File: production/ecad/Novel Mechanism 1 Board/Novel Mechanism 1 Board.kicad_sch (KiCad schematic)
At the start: 29 parts, among them J3 0532611271, U1 ADC081C021CIMM/NOPB, U2 ADC081C021CIMM/NOPB, U3 ADC081C021CIMM/NOPB

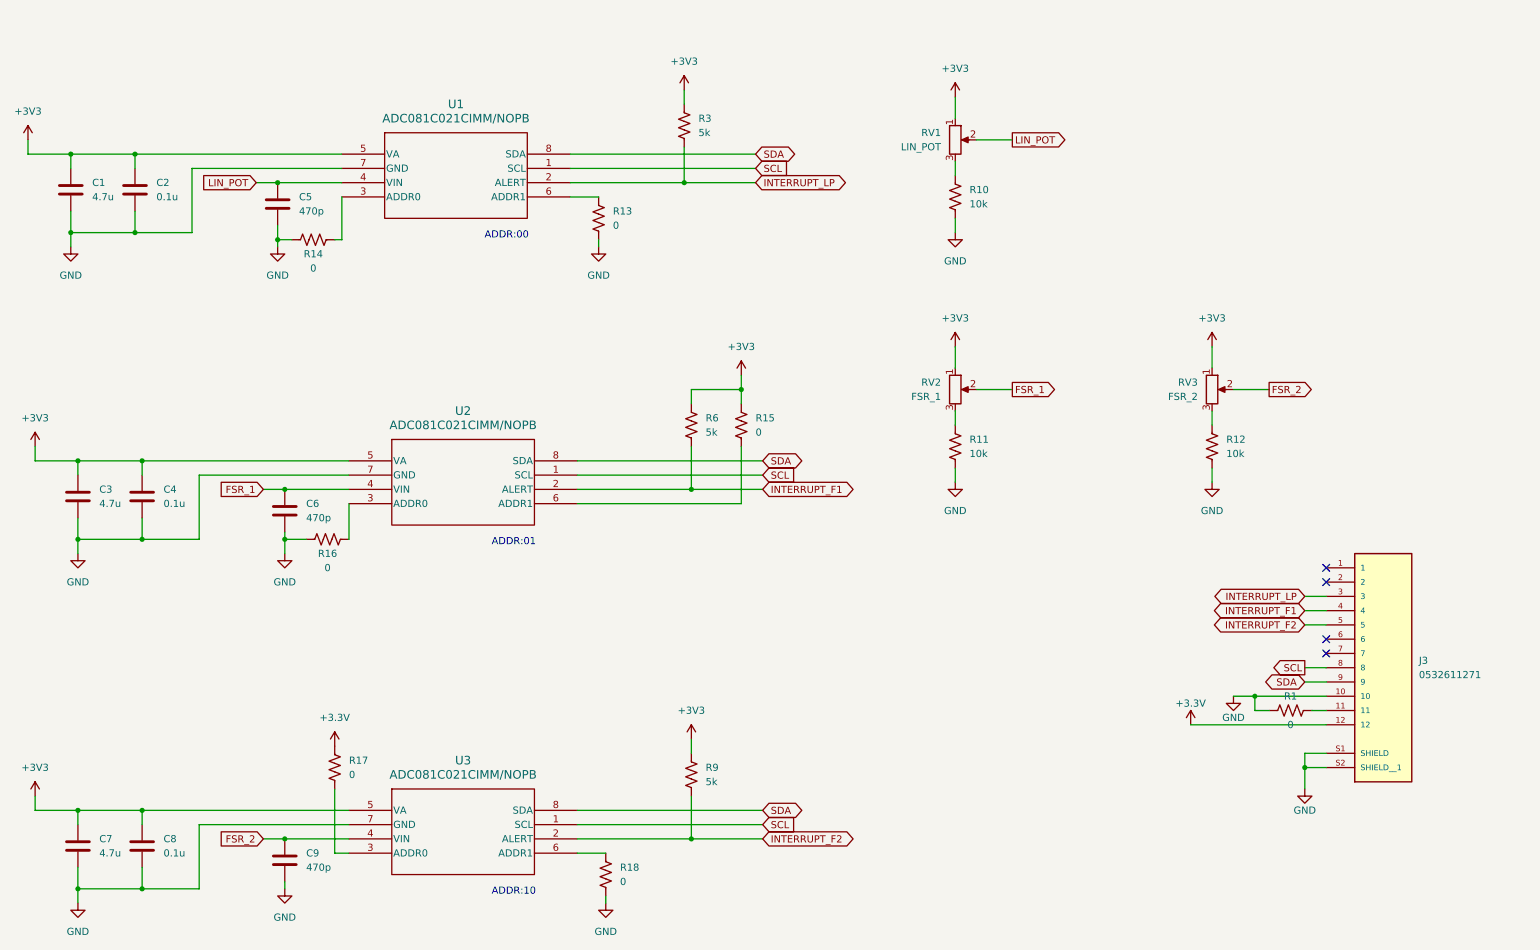
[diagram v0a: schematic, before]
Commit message: Finished Schematic for Vise Mechanism
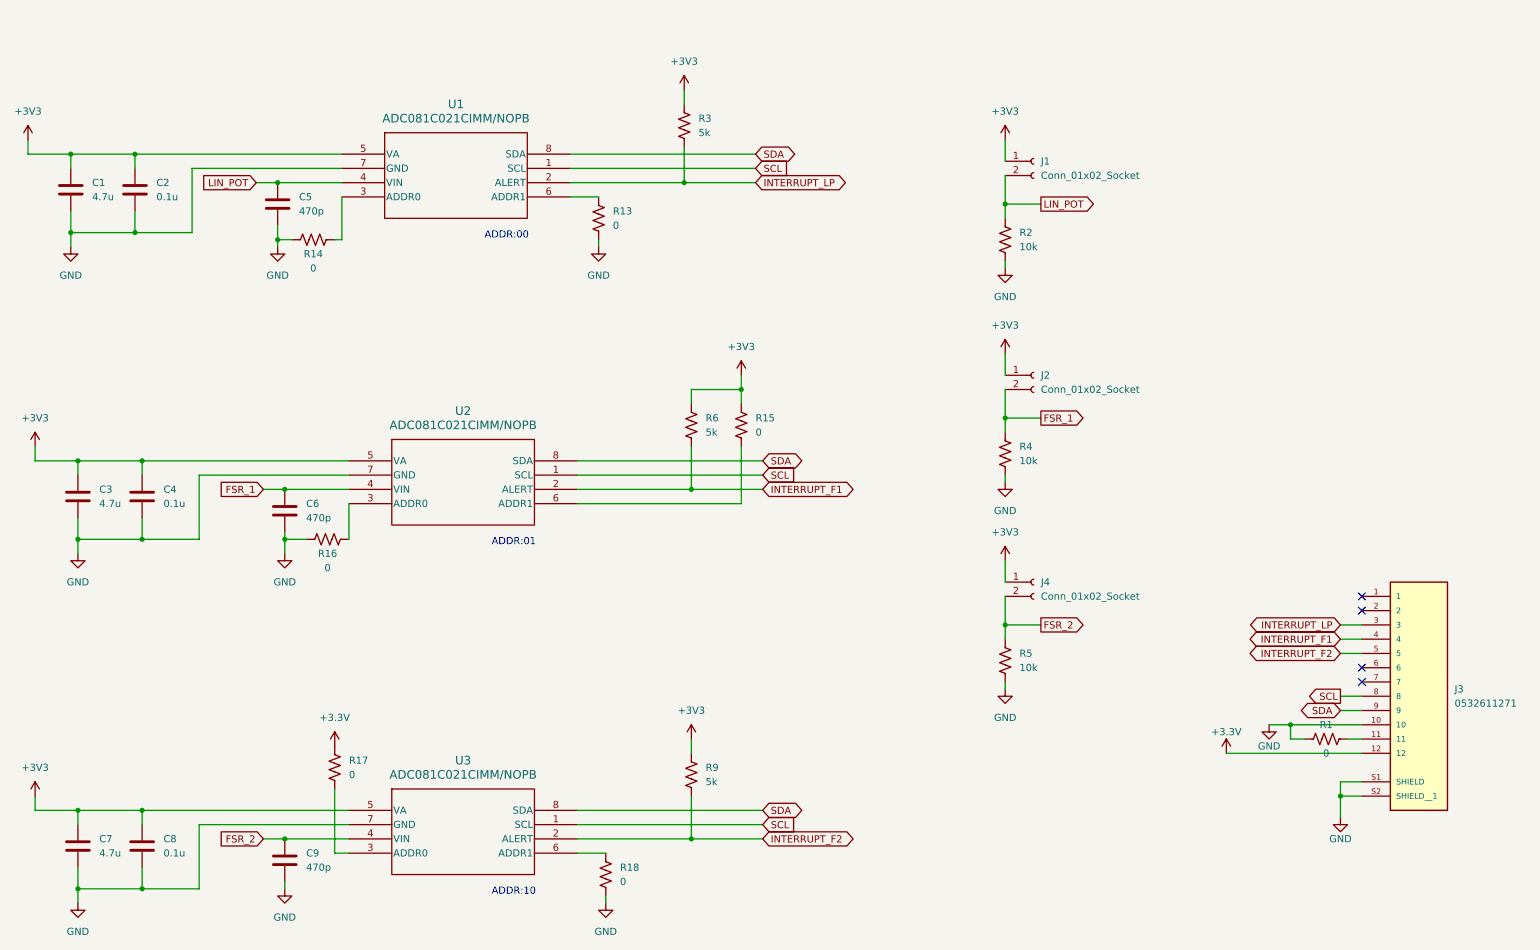
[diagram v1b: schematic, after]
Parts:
- removed R10, R11, R12: 10k, Resistor_SMD:R_0402_1005Metric, symbol Device:R_US
- removed RV1: LIN_POT, symbol Device:R_Potentiometer
- removed RV2: FSR_1, symbol Device:R_Potentiometer
- removed RV3: FSR_2, symbol Device:R_Potentiometer
- added J1, J2, J4: Conn_01x02_Socket, Connector_PinHeader_2.54mm:PinHeader_1x02_P2.54mm_Vertical, symbol Connector:Conn_01x02_Socket
- added R2, R4, R5: 10k, Resistor_SMD:R_0402_1005Metric, symbol Device:R_US
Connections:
- net +3V3: now also J1.1 (Pin_1), J2.1 (Pin_1), J4.1 (Pin_1)
- net FSR_1: now also J2.2 (Pin_2), R4.1
- net FSR_2: now also J4.2 (Pin_2), R5.1
- net GND: now also R2.2, R4.2, R5.2
- net LIN_POT: now also J1.2 (Pin_2), R2.1
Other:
- moved on the sheet: J3, R1

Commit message: Added Test Points and Mounting Holes for Vise Mechanism
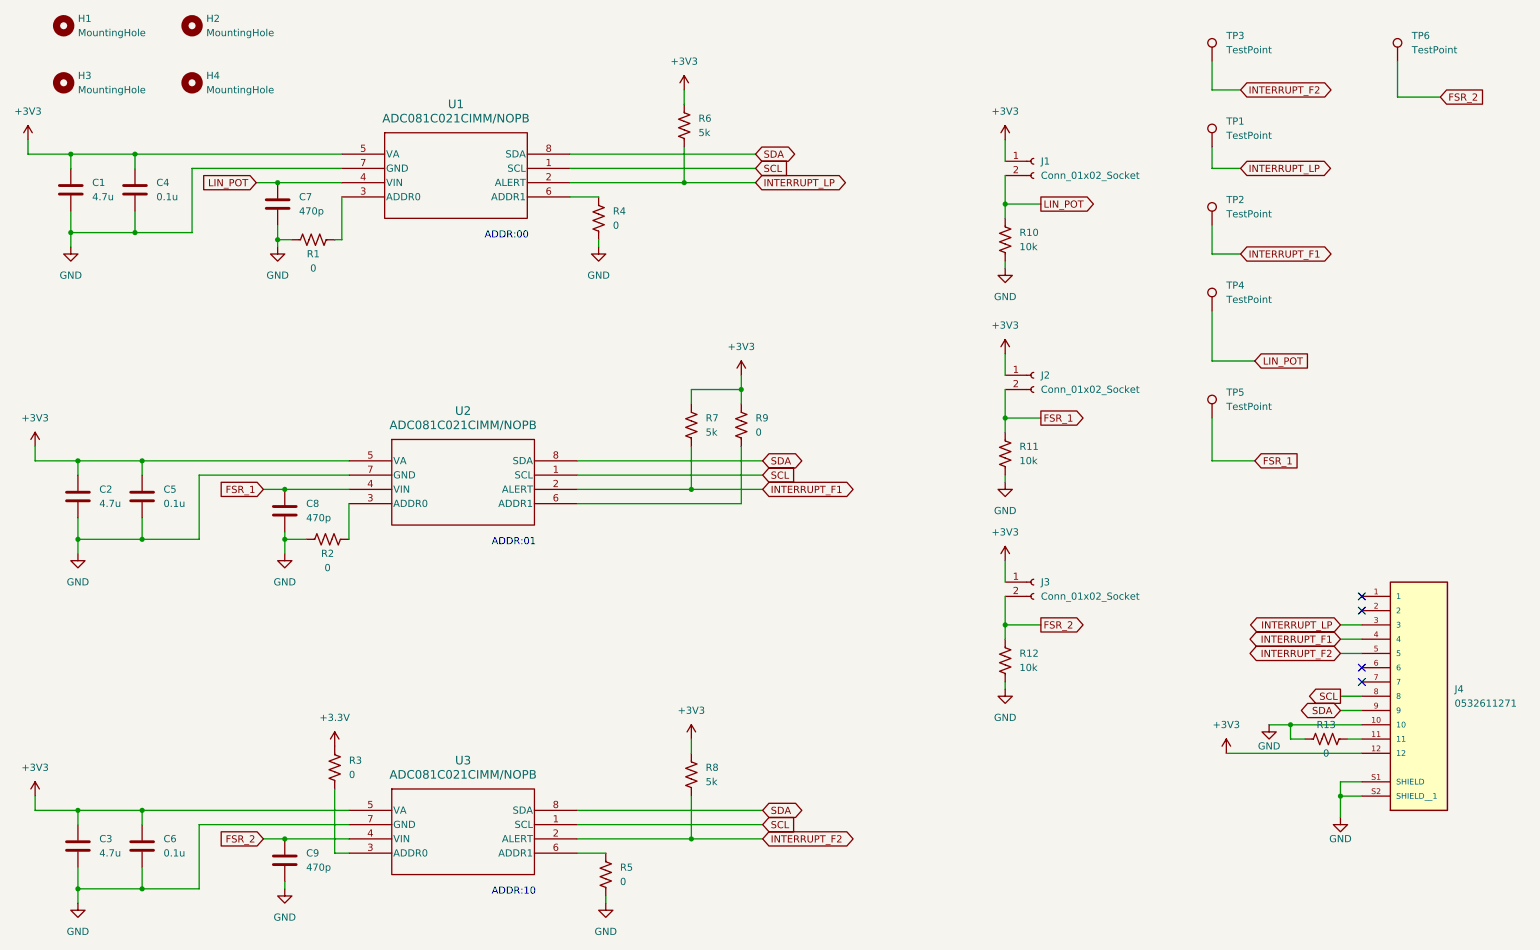
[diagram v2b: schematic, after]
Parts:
- added H1, H2, H3, H4: MountingHole, MountingHole:MountingHole_3.2mm_M3, symbol Mechanical:MountingHole
- added TP1, TP2, TP3, TP4, TP5, TP6: TestPoint, symbol Connector:TestPoint
- renumbered C3 to C2, C7 to C3, C2 to C4, C4 to C5, C8 to C6, C5 to C7, C6 to C8, J4 to J3, J3 to J4, R14 to R1, R2 to R10, R4 to R11, R5 to R12, R1 to R13, R16 to R2, R17 to R3, R13 to R4, R18 to R5, R3 to R6, R6 to R7, R9 to R8, R15 to R9
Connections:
- net +3.3V: no longer J4.12
- net +3V3: now also J4.12
- net FSR_1: now also TP5.1
- net FSR_2: now also TP6.1
- net INTERRUPT_F1: now also TP2.1
- net INTERRUPT_F2: now also TP3.1
- net INTERRUPT_LP: now also TP1.1
- net LIN_POT: now also TP4.1

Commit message: Forgot Testpoint Footprints lol
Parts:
- TP1: renamed from TP3; footprint (none) -> TestPoint:TestPoint_Pad_D2.0mm
- TP2: renamed from TP1; footprint (none) -> TestPoint:TestPoint_Pad_D2.0mm
- TP3: renamed from TP2; footprint (none) -> TestPoint:TestPoint_Pad_D2.0mm
- TP4, TP5, TP6: footprint (none) -> TestPoint:TestPoint_Pad_D2.0mm
- renumbered H3 to H2, H2 to H3
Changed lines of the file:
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@@
       (effects (font (size 1.27 1.27)) (justify left))
     )
-    (property "Footprint" "" (at 232.41 88.9 0)
+    (property "Footprint" "TestPoint:TestPoint_Pad_D2.0mm" (at 232.41 88.9 0)
       (effects (font (size 1.27 1.27)) hide)
     )
@@
   (symbol (lib_id "Connector:TestPoint") (at 227.33 25.4 0) (unit 1)
     (in_bom yes) (on_board yes) (dnp no) (fields_autoplaced)
-    (property "Reference" "TP3" (at 229.87 20.828 0)
+    (property "Reference" "TP1" (at 229.87 20.828 0)
       (effects (font (size 1.27 1.27)) (justify left))
     )
@@
       (effects (font (size 1.27 1.27)) (justify left))
     )
-    (property "Footprint" "" (at 232.41 25.4 0)
+    (property "Footprint" "TestPoint:TestPoint_Pad_D2.0mm" (at 232.41 25.4 0)
       (effects (font (size 1.27 1.27)) hide)
     )
@@
       (project "Novel Mechanism 1 Board"
         (path "/fd604e6b-a654-4356-8ca3-60ffdd33afe1"
-          (reference "TP3") (unit 1)
+          (reference "TP1") (unit 1)
         )
       )
@@
   (symbol (lib_id "Mechanical:MountingHole") (at 45.72 19.05 0) (unit 1)
     (in_bom yes) (on_board yes) (dnp no) (fields_autoplaced)
-    (property "Reference" "H2" (at 48.26 17.78 0)
+    (property "Reference" "H3" (at 48.26 17.78 0)
       (effects (font (size 1.27 1.27)) (justify left))
     )
@@
       (project "Novel Mechanism 1 Board"
         (path "/fd604e6b-a654-4356-8ca3-60ffdd33afe1"
-          (reference "H2") (unit 1)
+          (reference "H3") (unit 1)
         )
       )
@@
   (symbol (lib_id "Connector:TestPoint") (at 227.33 54.61 0) (unit 1)
     (in_bom yes) (on_board yes) (dnp no) (fields_autoplaced)
-    (property "Reference" "TP2" (at 229.87 50.038 0)
+    (property "Reference" "TP3" (at 229.87 50.038 0)
       (effects (font (size 1.27 1.27)) (justify left))
     )
@@
       (effects (font (size 1.27 1.27)) (justify left))
     )
-    (property "Footprint" "" (at 232.41 54.61 0)
+    (property "Footprint" "TestPoint:TestPoint_Pad_D2.0mm" (at 232.41 54.61 0)
       (effects (font (size 1.27 1.27)) hide)
     )
@@
       (project "Novel Mechanism 1 Board"
         (path "/fd604e6b-a654-4356-8ca3-60ffdd33afe1"
-          (reference "TP2") (unit 1)
+          (reference "TP3") (unit 1)
         )
       )
@@
   (symbol (lib_id "Connector:TestPoint") (at 227.33 40.64 0) (unit 1)
     (in_bom yes) (on_board yes) (dnp no) (fields_autoplaced)
-    (property "Reference" "TP1" (at 229.87 36.068 0)
+    (property "Reference" "TP2" (at 229.87 36.068 0)
       (effects (font (size 1.27 1.27)) (justify left))
     )
@@
       (effects (font (size 1.27 1.27)) (justify left))
     )
-    (property "Footprint" "" (at 232.41 40.64 0)
+    (property "Footprint" "TestPoint:TestPoint_Pad_D2.0mm" (at 232.41 40.64 0)
       (effects (font (size 1.27 1.27)) hide)
     )
@@
       (project "Novel Mechanism 1 Board"
         (path "/fd604e6b-a654-4356-8ca3-60ffdd33afe1"
-          (reference "TP1") (unit 1)
+          (reference "TP2") (unit 1)
         )
       )
@@
       (effects (font (size 1.27 1.27)) (justify left))
     )
-    (property "Footprint" "" (at 232.41 69.85 0)
+    (property "Footprint" "TestPoint:TestPoint_Pad_D2.0mm" (at 232.41 69.85 0)
       (effects (font (size 1.27 1.27)) hide)
     )
@@
       (effects (font (size 1.27 1.27)) (justify left))
     )
-    (property "Footprint" "" (at 265.43 25.4 0)
+    (property "Footprint" "TestPoint:TestPoint_Pad_D2.0mm" (at 265.43 25.4 0)
       (effects (font (size 1.27 1.27)) hide)
     )
@@
   (symbol (lib_id "Mechanical:MountingHole") (at 22.86 29.21 0) (unit 1)
     (in_bom yes) (on_board yes) (dnp no) (fields_autoplaced)
-    (property "Reference" "H3" (at 25.4 27.94 0)
+    (property "Reference" "H2" (at 25.4 27.94 0)
       (effects (font (size 1.27 1.27)) (justify left))
     )
@@
       (project "Novel Mechanism 1 Board"
         (path "/fd604e6b-a654-4356-8ca3-60ffdd33afe1"
-          (reference "H3") (unit 1)
-        )
-      )
+          (reference "H2") (unit 1)
+        )
+      )

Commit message: changed pin 10 to not ground
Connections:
- net GND: no longer J4.10
- no-connect marks 4 -> 5
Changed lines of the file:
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@@
   (junction (at 60.96 46.99) (diameter 0) (color 0 0 0 0)
-  )
-  (junction (at 241.3 143.51) (diameter 0) (color 0 0 0 0)
   )
   (junction (at 35.56 41.91) (diameter 0) (color 0 0 0 0)
@@
   (no_connect (at 254 123.19))
   (no_connect (at 254 135.89))
+  (no_connect (at 254 143.51))
   (no_connect (at 254 120.65))
   (no_connect (at 254 133.35))
@@
     (stroke (width 0) (type default))
   )
-  (wire (pts (xy 241.3 143.51) (xy 254 143.51))
-    (stroke (width 0) (type default))
-  )

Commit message: resolving errors
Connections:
- net +3.3V is gone; now on net +3V3: R3.1
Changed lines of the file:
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@@
+    )
+  )
+  (symbol (lib_id "power:+3V3") (at 71.12 147.32 0) (unit 1)
+    (in_bom yes) (on_board yes) (dnp no) (fields_autoplaced)
+    (property "Reference" "#PWR010" (at 71.12 151.13 0)
+      (effects (font (size 1.27 1.27)) hide)
+    )
+    (property "Value" "+3V3" (at 71.12 142.24 0)
+      (effects (font (size 1.27 1.27)))
+    )
+    (property "Footprint" "" (at 71.12 147.32 0)
+      (effects (font (size 1.27 1.27)) hide)
+    )
+    (property "Datasheet" "" (at 71.12 147.32 0)
+      (effects (font (size 1.27 1.27)) hide)
+    )
+    (pin "1")
+    (instances
+      (project "Novel Mechanism 1 Board"
+        (path "/fd604e6b-a654-4356-8ca3-60ffdd33afe1"
+          (reference "#PWR010") (unit 1)
+        )
+      )
     )
   )
@@
         )
       )
-    )
-  )
-  (symbol (lib_id "power:+3.3V") (at 71.12 147.32 0) (unit 1)
-    (in_bom yes) (on_board yes) (dnp no) (fields_autoplaced)
-    (property "Reference" "#PWR010" (at 71.12 151.13 0)
-      (effects (font (size 1.27 1.27)) hide)
-    )
-    (property "Value" "+3.3V" (at 71.12 142.24 0)
-      (effects (font (size 1.27 1.27)))
-    )
-    (property "Footprint" "" (at 71.12 147.32 0)
-      (effects (font (size 1.27 1.27)) hide)
-    )
-    (property "Datasheet" "" (at 71.12 147.32 0)
-      (effects (font (size 1.27 1.27)) hide)
-    )
-    (pin "1")
-    (instances
-      (project "Novel Mechanism 1 Board"
-        (path "/fd604e6b-a654-4356-8ca3-60ffdd33afe1"
-          (reference "#PWR010") (unit 1)
-        )
-      )
